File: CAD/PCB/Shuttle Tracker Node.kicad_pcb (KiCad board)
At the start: 2 copper layers, 15 parts

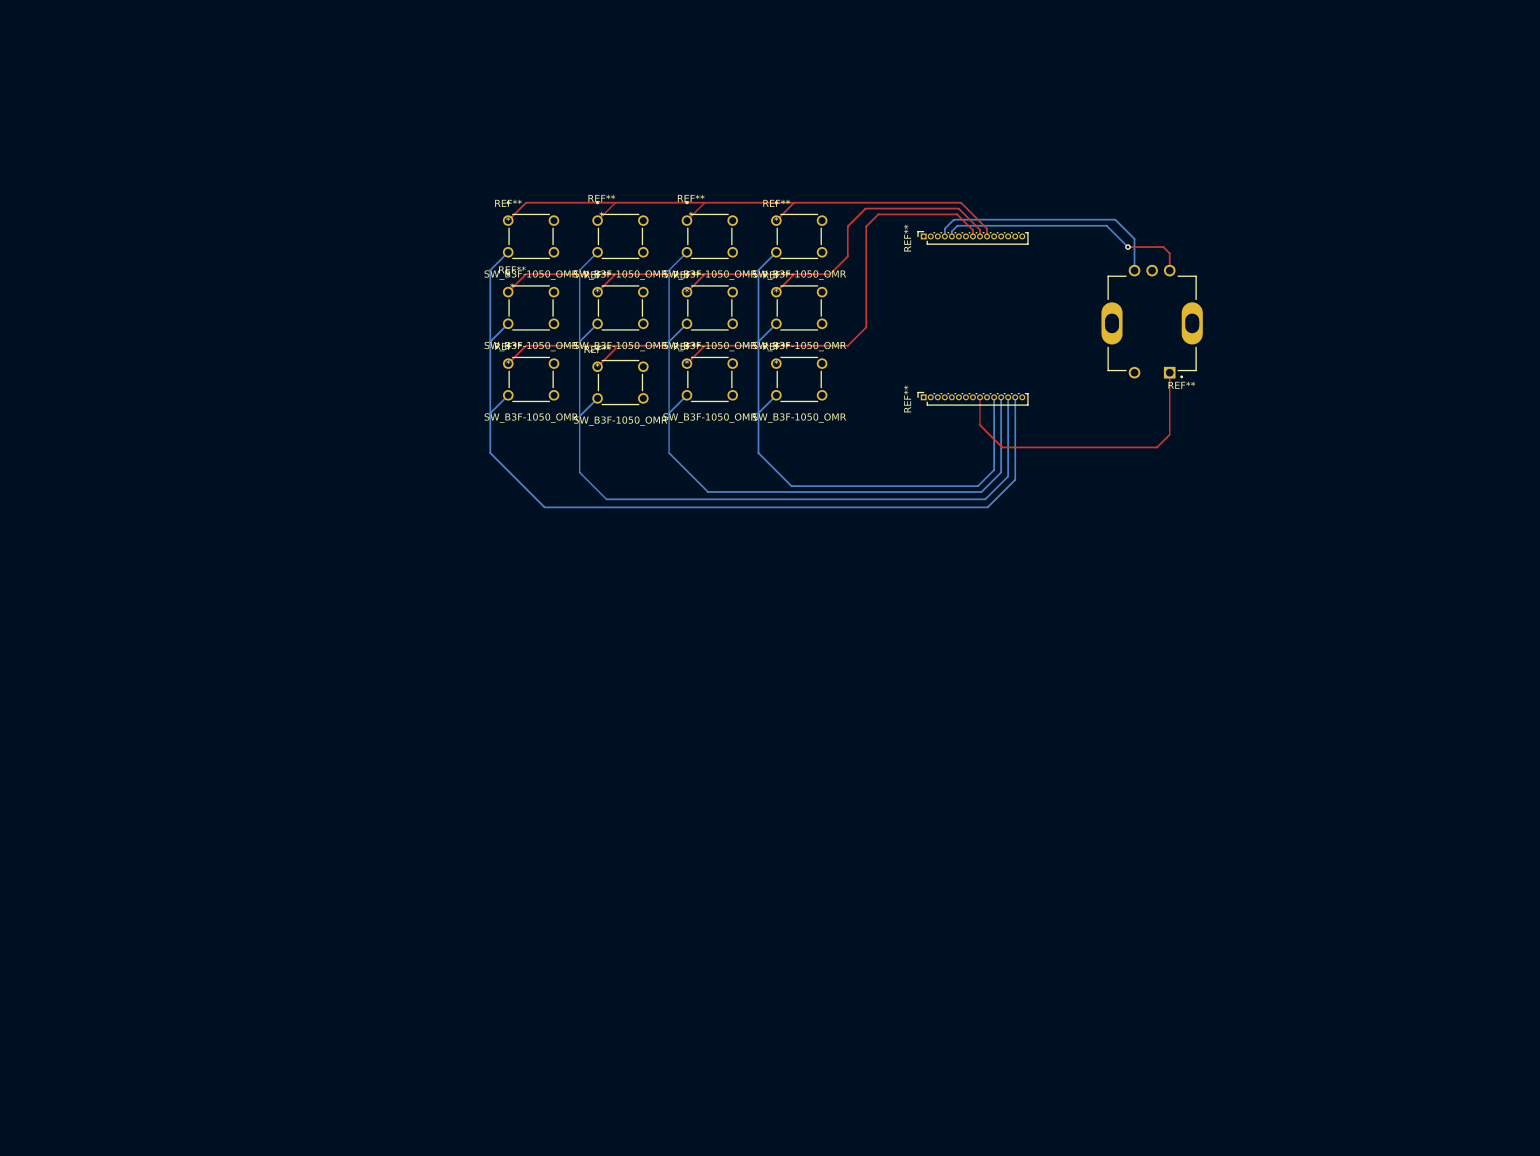
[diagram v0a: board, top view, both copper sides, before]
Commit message: Finished PCB Schematic
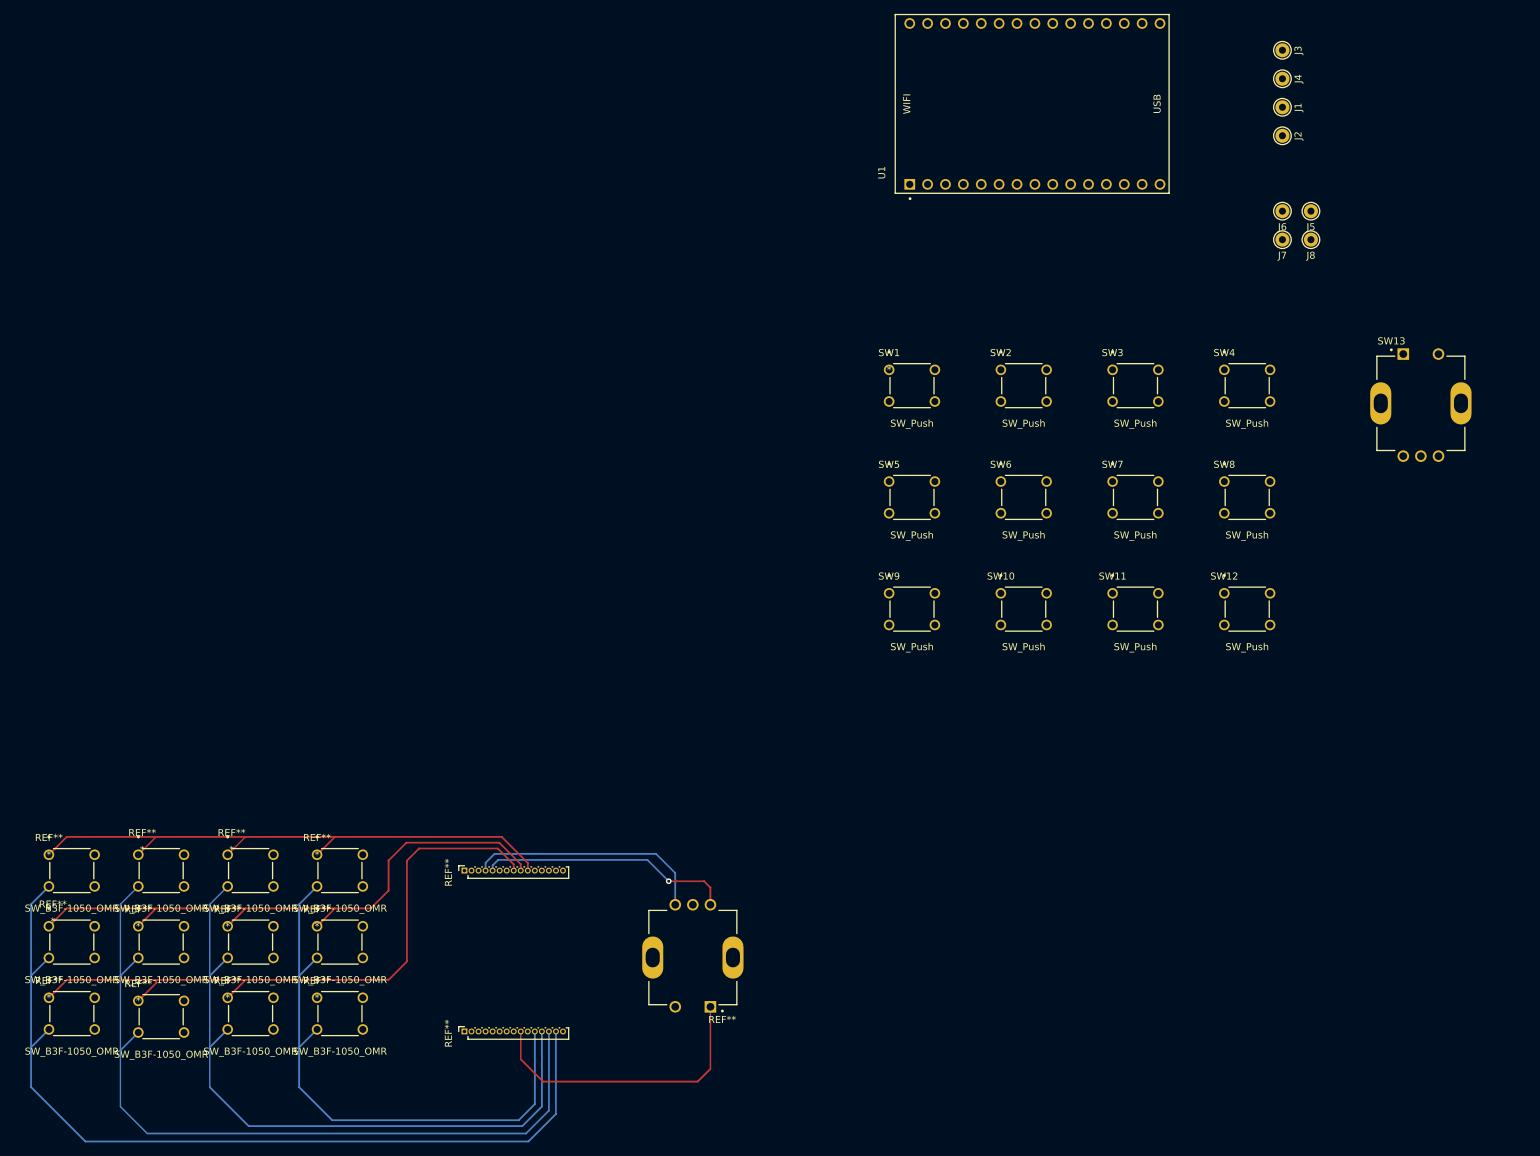
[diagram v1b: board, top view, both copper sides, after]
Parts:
- added J1: Conn_01x01, Connector_Pin:Pin_D1.0mm_L10.0mm, F.Cu at (195.6, 43.7)
- added J2: Conn_01x01, Connector_Pin:Pin_D1.0mm_L10.0mm, F.Cu at (195.6, 47.7)
- added J3: Conn_01x01, Connector_Pin:Pin_D1.0mm_L10.0mm, F.Cu at (195.6, 35.6)
- added J4: Conn_01x01, Connector_Pin:Pin_D1.0mm_L10.0mm, F.Cu at (195.6, 39.6)
- added J5: Conn_01x01, Connector_Pin:Pin_D1.0mm_L10.0mm, F.Cu at (199.6, 58.4)
- added J6: Conn_01x01, Connector_Pin:Pin_D1.0mm_L10.0mm, F.Cu at (195.6, 58.4)
- added J7: Conn_01x01, Connector_Pin:Pin_D1.0mm_L10.0mm, F.Cu at (195.6, 62.5)
- added J8: Conn_01x01, Connector_Pin:Pin_D1.0mm_L10.0mm, F.Cu at (199.6, 62.5)
- added SW1: SW_Push, B3F-1056:B3F-1056, F.Cu at (139.7, 81.0)
- added SW10: SW_Push, B3F-1056:B3F-1056, F.Cu at (155.6, 112.7)
- added SW11: SW_Push, B3F-1056:B3F-1056, F.Cu at (171.4, 112.7)
- added SW12: SW_Push, B3F-1056:B3F-1056, F.Cu at (187.3, 112.7)
- added SW13: PEC11-4215F-S24, PEC11R-4215F-S0024:PEC11R-4215F-S0024, F.Cu at (215.2, 85.7)
- added SW2: SW_Push, B3F-1056:B3F-1056, F.Cu at (155.6, 81.0)
- added SW3: SW_Push, B3F-1056:B3F-1056, F.Cu at (171.4, 81.0)
- added SW4: SW_Push, B3F-1056:B3F-1056, F.Cu at (187.3, 81.0)
- added SW5: SW_Push, B3F-1056:B3F-1056, F.Cu at (139.7, 96.8)
- added SW6: SW_Push, B3F-1056:B3F-1056, F.Cu at (155.6, 96.8)
- added SW7: SW_Push, B3F-1056:B3F-1056, F.Cu at (171.4, 96.8)
- added SW8: SW_Push, B3F-1056:B3F-1056, F.Cu at (187.3, 96.8)
- added SW9: SW_Push, B3F-1056:B3F-1056, F.Cu at (139.7, 112.7)
- added U1: ESP32-C3-DEVKITC-02, ESP32-C3-DEVKITC-02:XCVR_ESP32-C3-DEVKITC-02, F.Cu at (160.0, 43.2)
- moved REF** 111.2 mm to (45.7, 149.9)
- moved REF** 111.2 mm to (58.4, 160.0)
- moved REF** 111.2 mm to (58.4, 149.9)
- moved REF** 111.2 mm to (79.4, 152.1)
- moved REF** 111.2 mm to (45.7, 160.0)
- moved REF** 111.2 mm to (20.3, 170.2)
- moved REF** 111.2 mm to (20.3, 160.0)
- moved REF** 111.2 mm to (33.0, 160.0)
- moved REF** 111.2 mm to (45.7, 170.2)
- moved REF** 111.2 mm to (20.3, 149.9)
- moved REF** 111.2 mm to (33.0, 149.9)
- moved REF** 111.2 mm to (79.4, 175.0)
- moved REF** 111.2 mm to (58.4, 170.2)
- moved REF** 111.2 mm to (33.0, 170.6)
- moved REF** 111.2 mm to (111.8, 164.5)

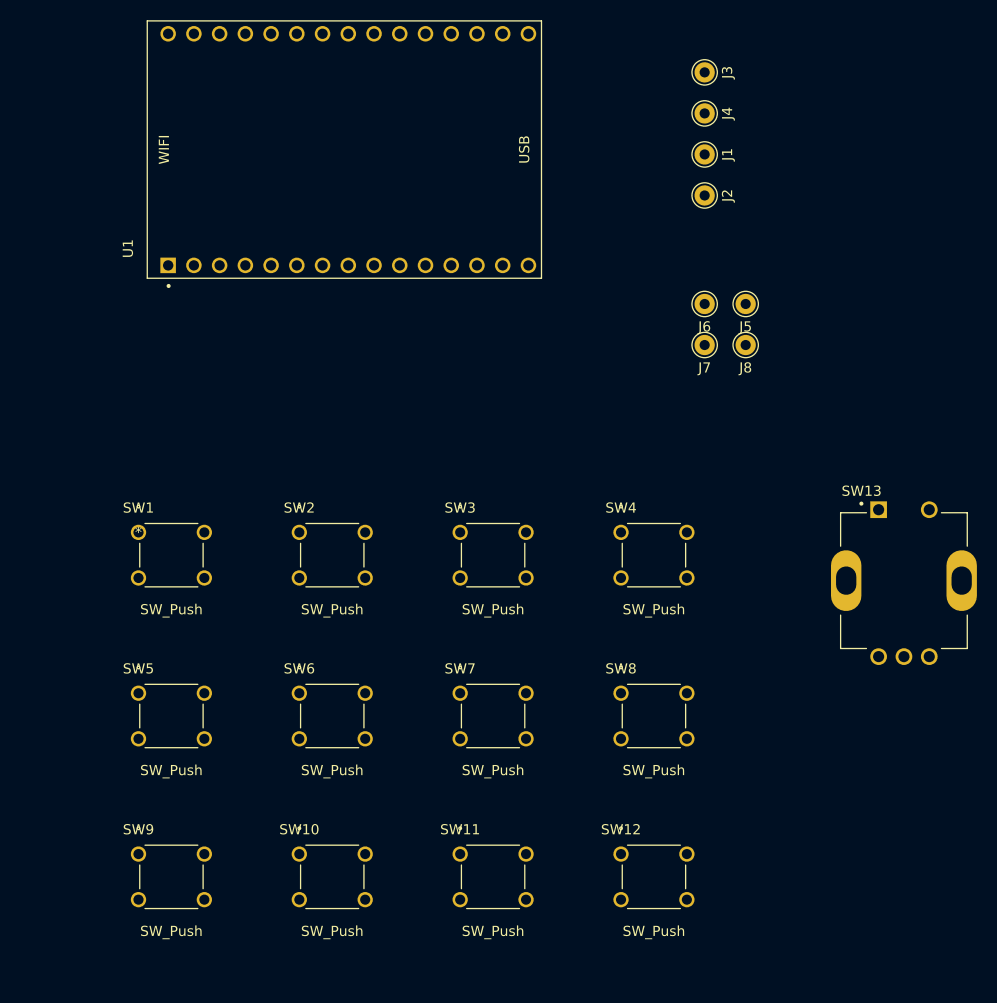
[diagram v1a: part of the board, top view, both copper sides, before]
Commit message: Place Components on PCB
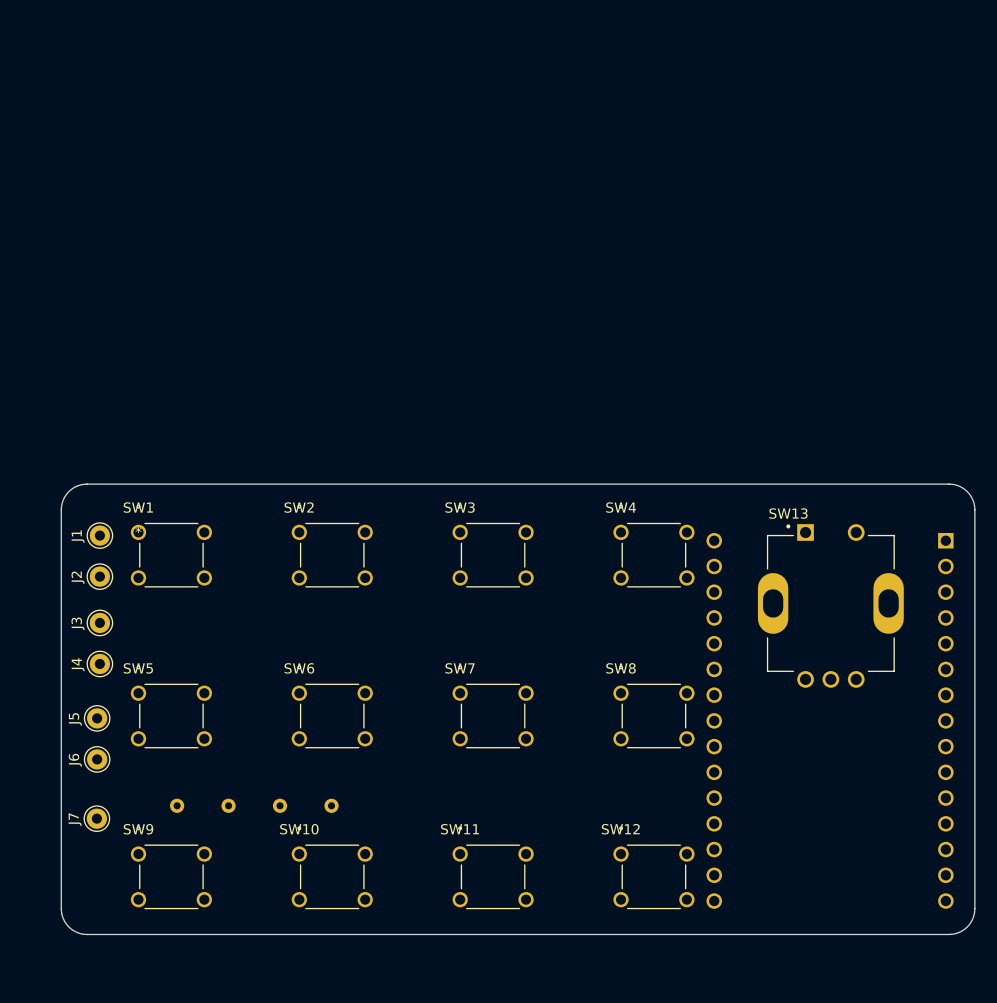
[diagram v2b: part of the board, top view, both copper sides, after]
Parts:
- removed J8: Conn_01x01, Connector_Pin:Pin_D1.0mm_L10.0mm
- added R1: R_Small_US, Resistor_THT:R_Axial_DIN0204_L3.6mm_D1.6mm_P5.08mm_Horizontal, B.Cu at (143.5, 108.0)
- added R2: R_Small_US, Resistor_THT:R_Axial_DIN0204_L3.6mm_D1.6mm_P5.08mm_Horizontal, B.Cu at (153.7, 108.0)
- U1: moved to B.Cu
- moved J3 80.7 mm to (135.9, 89.9), turned to -90 degrees
- moved J4 80.7 mm to (135.9, 94.0), turned to -90 degrees
- moved J7 76.1 mm to (135.6, 109.2), turned to -90 degrees
- moved J5 76.0 mm to (135.6, 99.3), turned to -90 degrees
- moved J6 74.9 mm to (135.6, 103.4), turned to -90 degrees
- moved U1 73.7 mm to (208.0, 99.2), turned to 180 degrees
- moved J1 70.6 mm to (135.9, 81.3), turned to -90 degrees
- moved J2 70.6 mm to (135.9, 85.3), turned to -90 degrees
- moved SW13 7.56 mm to (208.0, 88.0)
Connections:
- J7 pad 1: LCD_5V -> V_IN
- U1 pad 13: unconnected-(U1-Pad13) -> LCD_5V
- U1 pad 16: unconnected-(U1-Pad16) -> LCD_GND
- U1 pad 17: unconnected-(U1-Pad17) -> V_GND
- U1 pad 6: R1 -> V_OUT
- U1 pad 7: R2 -> R1
- U1 pad 8: R3 -> R2
- U1 pad 9: unconnected-(U1-Pad9) -> R3
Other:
- board outline added: 90.2 x 44.5 mm

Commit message: Finished PCB Routing
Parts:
- removed REF** (x12): SW_B3F-1050_OMR, B3F-1056:B3F-1056
- removed REF** (x2): PinSocket_1x15_P1.00mm_Vertical, Connector_PinSocket_1.00mm:PinSocket_1x15_P1.00mm_Vertical
- removed REF**: PEC11R-4215F-S0024, PEC11R-4215F-S0024:PEC11R-4215F-S0024
- moved R2 30.4 mm to (126.3, 121.2), turned to 90 degrees
- moved J5 26.4 mm to (109.5, 103.0)
- moved J6 26.4 mm to (109.5, 107.1)
- moved J7 26.4 mm to (109.5, 112.9)
- moved J1 26.4 mm to (109.7, 85.0)
- moved J2 26.4 mm to (109.7, 89.0)
- moved J3 26.4 mm to (109.7, 93.6)
- moved J4 26.4 mm to (109.7, 97.7)
- moved SW1 26.4 mm to (113.6, 84.7)
- moved SW10 26.4 mm to (129.4, 116.4)
- moved SW11 26.4 mm to (145.3, 116.4)
- moved SW12 26.4 mm to (161.2, 116.4)
- moved SW13 26.4 mm to (181.9, 91.7)
- moved SW2 26.4 mm to (129.4, 84.7)
- moved SW3 26.4 mm to (145.3, 84.7)
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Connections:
- U1 pad 11: ENC_A -> ENC_B
- U1 pad 12: ENC_B -> ENC_A
- U1 pad 26: C4 -> C1
- U1 pad 27: C3 -> C2
- U1 pad 28: C2 -> C3
- U1 pad 29: C1 -> C4
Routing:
- net (no net): track 802.8 -> 0.00 mm, vias 1 -> 0
- net LCD_5V: track 0.00 -> 125.6 mm
- net C1: track 0.00 -> 110.4 mm
- net BAT_5V: track 0.00 -> 109.6 mm
- net BAT_GND: track 0.00 -> 99.5 mm
- net R1: track 0.00 -> 93.2 mm
- net C2: track 0.00 -> 90.0 mm
- net LCD_GND: track 0.00 -> 89.0 mm, vias 0 -> 1
- net V_OUT: track 0.00 -> 87.1 mm
- net LCD_DAT: track 0.00 -> 84.8 mm, vias 0 -> 1
- net R3: track 0.00 -> 83.9 mm
- net R2: track 0.00 -> 82.0 mm
- net LCD_CLK: track 0.00 -> 80.8 mm
- net C3: track 0.00 -> 70.7 mm
- net C4: track 0.00 -> 50.6 mm
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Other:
- board size 90.2 x 44.5 mm -> 90.8 x 45.7 mm
- board text added: "1.0.0"
- board text added: "Shuttle Tracker Node"

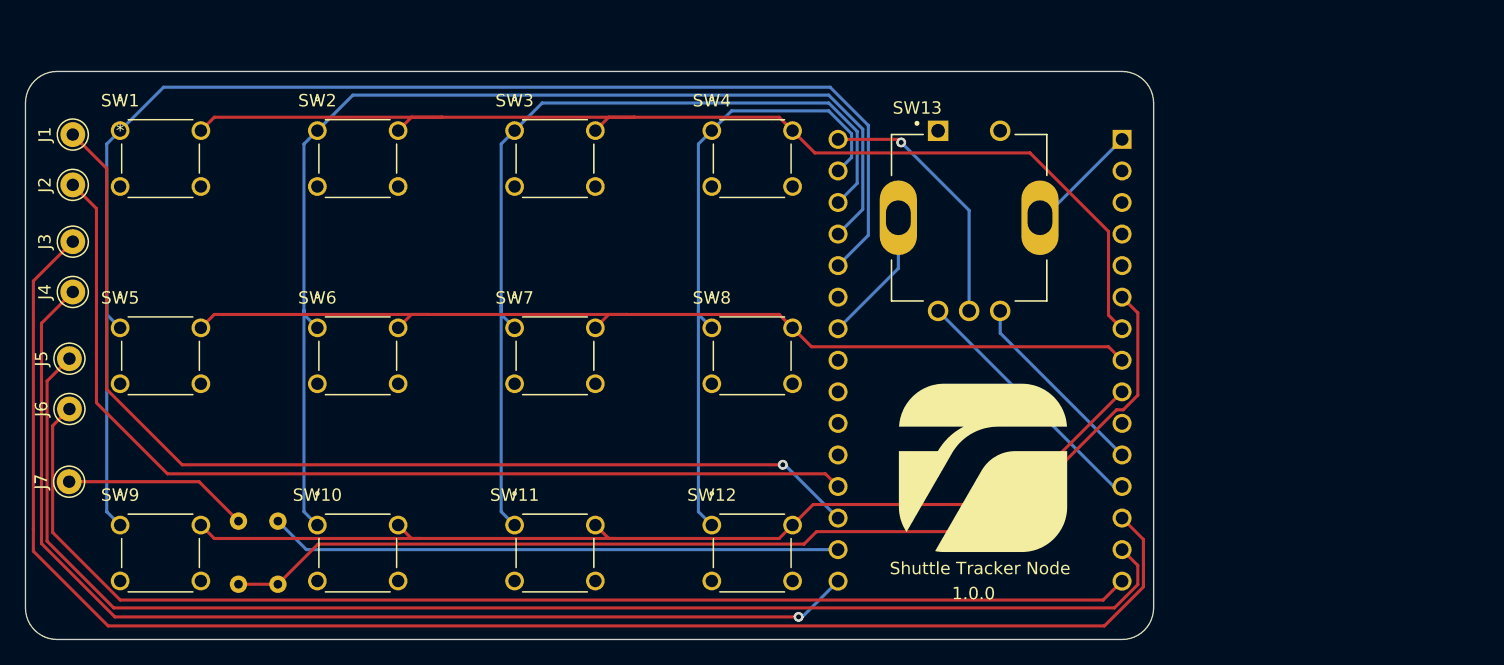
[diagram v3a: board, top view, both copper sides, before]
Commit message: Added Silkscreen
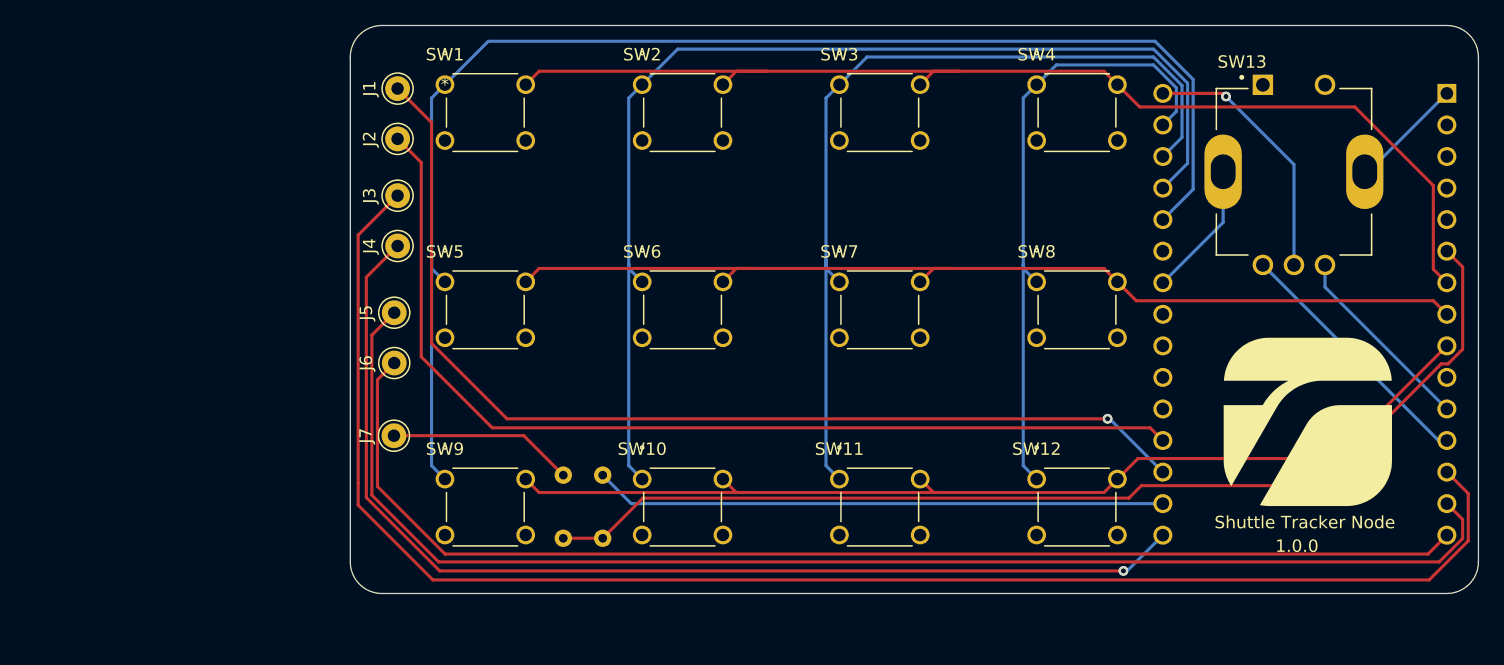
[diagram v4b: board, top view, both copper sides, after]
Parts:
- moved J5 26.4 mm to (135.6, 99.3)
- moved J6 26.4 mm to (135.6, 103.4)
- moved J7 26.4 mm to (135.6, 109.2)
- moved R2 26.4 mm to (152.4, 117.5)
- moved J1 26.4 mm to (135.9, 81.3)
- moved J2 26.4 mm to (135.9, 85.3)
- moved J3 26.4 mm to (135.9, 89.9)
- moved J4 26.4 mm to (135.9, 94.0)
- moved R1 26.4 mm to (149.2, 112.4)
- moved SW1 26.4 mm to (139.7, 81.0)
- moved SW10 26.4 mm to (155.6, 112.7)
- moved SW11 26.4 mm to (171.4, 112.7)
- moved SW12 26.4 mm to (187.3, 112.7)
- moved SW13 26.4 mm to (208.0, 88.0)
- moved SW2 26.4 mm to (155.6, 81.0)
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
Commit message: PCB Routing Updates
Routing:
- net R1: track 93.2 -> 110.5 mm
- net R3: track 83.9 -> 94.1 mm
- net R2: track 82.0 -> 90.1 mm
- net C1: track 110.4 -> 102.6 mm
- net LCD_5V: track 125.6 -> 118.3 mm
- net C2: track 90.0 -> 84.7 mm
- net BAT_5V: track 109.6 -> 114.3 mm
- net V_OUT: track 87.1 -> 91.2 mm, vias 0 -> 1
- net LCD_CLK: track 80.8 -> 78.4 mm
- net BAT_GND: track 99.5 -> 101.8 mm
- net C3: track 70.7 -> 68.4 mm
- net LCD_GND: track 89.0 -> 87.1 mm, vias 1 -> 0
- net LCD_DAT: track 84.8 -> 83.6 mm
- net C4: track 50.6 -> 51.7 mm
- net ENC_A: track 20.7 -> 21.5 mm
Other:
- board text added: "1.0.1"
- board text removed: "1.0.0"
